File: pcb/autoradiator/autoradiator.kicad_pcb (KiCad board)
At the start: 2 copper layers, 66 x 43.2 mm, 12 parts, among them J1 Barrel Jack, J2 Motor Hdr, U1 ChineseDCDCBoard, U2 WeMos_D1_mini, U3 DRV8870DDA

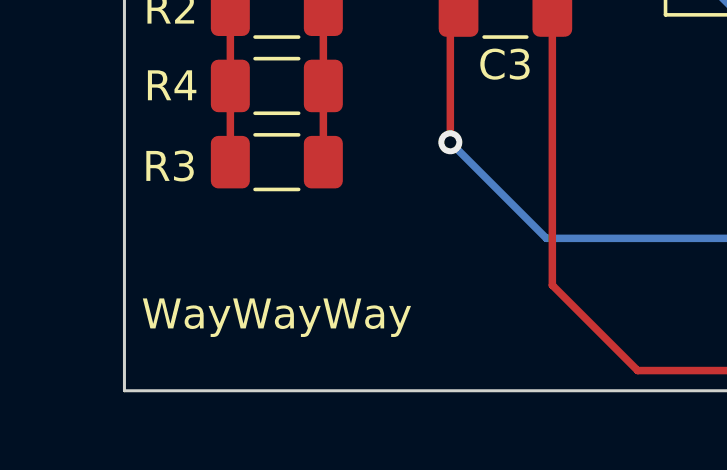
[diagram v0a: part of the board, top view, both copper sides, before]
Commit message: Updated PCB to mark some resistors as not populated
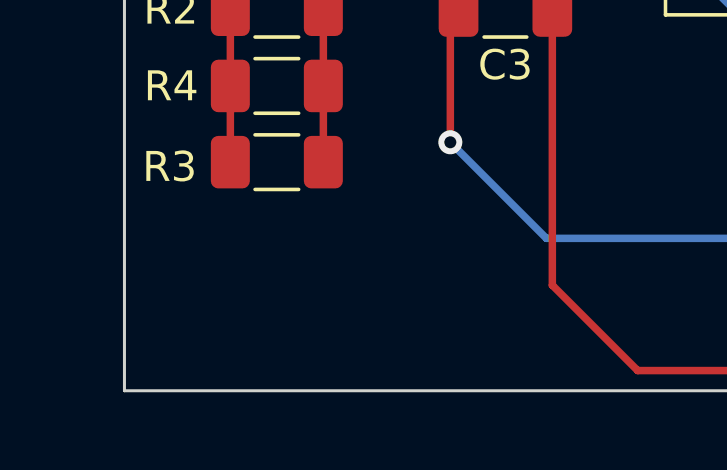
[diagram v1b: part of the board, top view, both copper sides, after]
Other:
- board text removed: "WayWayWay"
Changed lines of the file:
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@@
   )
   (gr_rect (start 96.52 111.76) (end 30.48 68.58) (layer "Edge.Cuts") (width 0.1) (fill none))
-  (gr_text "WayWayWay" (at 35.56 109.22) (layer "F.SilkS")
-    (effects (font (size 1 1) (thickness 0.15)))
-  )
   (gr_text "Autoradiator-- nicholasroth.net" (at 43.581293 70.217342) (layer "F.SilkS")
     (effects (font (size 1 1) (thickness 0.15)))
